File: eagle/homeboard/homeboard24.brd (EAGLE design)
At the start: 94 x 71.8 mm, 128 parts, among them IC1 XCF02S, IC2 25LC080SN, IC3 ATMEGA32U2-TQFP, Q5 BC848SMD, Q6 BC848SMD, Q7 BC848SMD, Q8 BC848SMD, T1 BSS138, T2 BC848, T3 BSS138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

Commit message: added text
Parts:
- removed C28, C30, C31: 100nF, rcl:C0603
- moved C13 36.1 mm to (64.5, 41.5), flipped to the bottom, turned to 180 degrees
- moved U$8 1.12 mm to (89.5, 51.0)
- moved R36 1.00 mm to (55.2, 54.5)
- moved R39 1.00 mm to (57.5, 54.5)
- moved R46 1.00 mm to (53.0, 54.5)
- moved U$7 0.50 mm to (4.50, 55.0)
- moved U$9 0.50 mm to (89.5, 10.0)
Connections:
- net GND: no longer C28.2, C30.2, C31.2
- net VCC: no longer C28.1, C30.1, C31.1
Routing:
- net GND: track 999.5 -> 1001.9 mm
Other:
- board text added: "#crtc"
- board text added: "(c) 2012 Ranulf Doswell"
- board text added: "-FPGA-XTAL-"
- board text added: "123"
- board text added: "127"
- board text added: "128"
- board text added: "129"
- board text added: "130"
- board text added: "132"
- board text added: "135"
- board text added: "137"
- board text added: "5V"
- board text added: "CPCFPGA.COM rev 1"
- board text added: "GND"
- board text added: "P47"
- board text added: "P50"
- board text added: "P51"
- board text added: "P74"
- board text added: "P76"
- board text added: "P77"
- board text added: "VCC"
- board text added: "VCCAUX"
- board text added: "VCCINT"

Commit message: mah
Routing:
- net VCC: track 533.5 -> 539.5 mm
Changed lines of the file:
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@@
 <wire x1="36.25" y1="44.75" x2="23.5" y2="44.75" width="0.7" layer="1"/>
 <wire x1="23.5" y1="44.75" x2="23.5" y2="47.5" width="0.7" layer="1"/>
-<wire x1="23.5" y1="47.5" x2="16.5" y2="47.5" width="0.7" layer="1"/>
+<wire x1="23.5" y1="47.5" x2="23.5" y2="53.55" width="0.7" layer="1"/>
 <wire x1="16.5" y1="47.5" x2="13" y2="47.5" width="0.7" layer="1"/>
 <wire x1="13" y1="47.5" x2="9.5" y2="47.5" width="0.8" layer="1"/>
@@
 <wire x1="83.5" y1="20.75" x2="85.5" y2="20.75" width="0.8" layer="1"/>
 <contactref element="SV4" pad="20"/>
-<wire x1="21.75" y1="53.55" x2="24" y2="53.55" width="0.7" layer="1"/>
+<wire x1="21.75" y1="53.55" x2="23.5" y2="53.55" width="0.7" layer="1"/>
+<wire x1="23.5" y1="53.55" x2="24" y2="53.55" width="0.7" layer="1"/>
 <wire x1="24" y1="53.55" x2="26.25" y2="53.55" width="0.7" layer="1"/>
 <wire x1="26.25" y1="53.55" x2="28.5" y2="53.55" width="0.7" layer="1"/>
@@
 <wire x1="64.5" y1="53.5" x2="64.7" y2="53.5" width="0.254" layer="1"/>
 <wire x1="64.7" y1="53.5" x2="64.75" y2="53.55" width="0.254" layer="1"/>
-<wire x1="37.5" y1="15.75" x2="37.52" y2="15.79" width="0" layer="19" extent="1-1"/>
-<wire x1="23.516" y1="17.9906" x2="23.5" y2="18" width="0" layer="19" extent="16-16"/>
+<wire x1="16.5" y1="47.5" x2="23.5" y2="47.5" width="0.6" layer="1"/>
+<wire x1="23.5" y1="18" x2="23.516" y2="17.9906" width="0" layer="19" extent="16-16"/>
 </signal>
 <signal name="TCK">

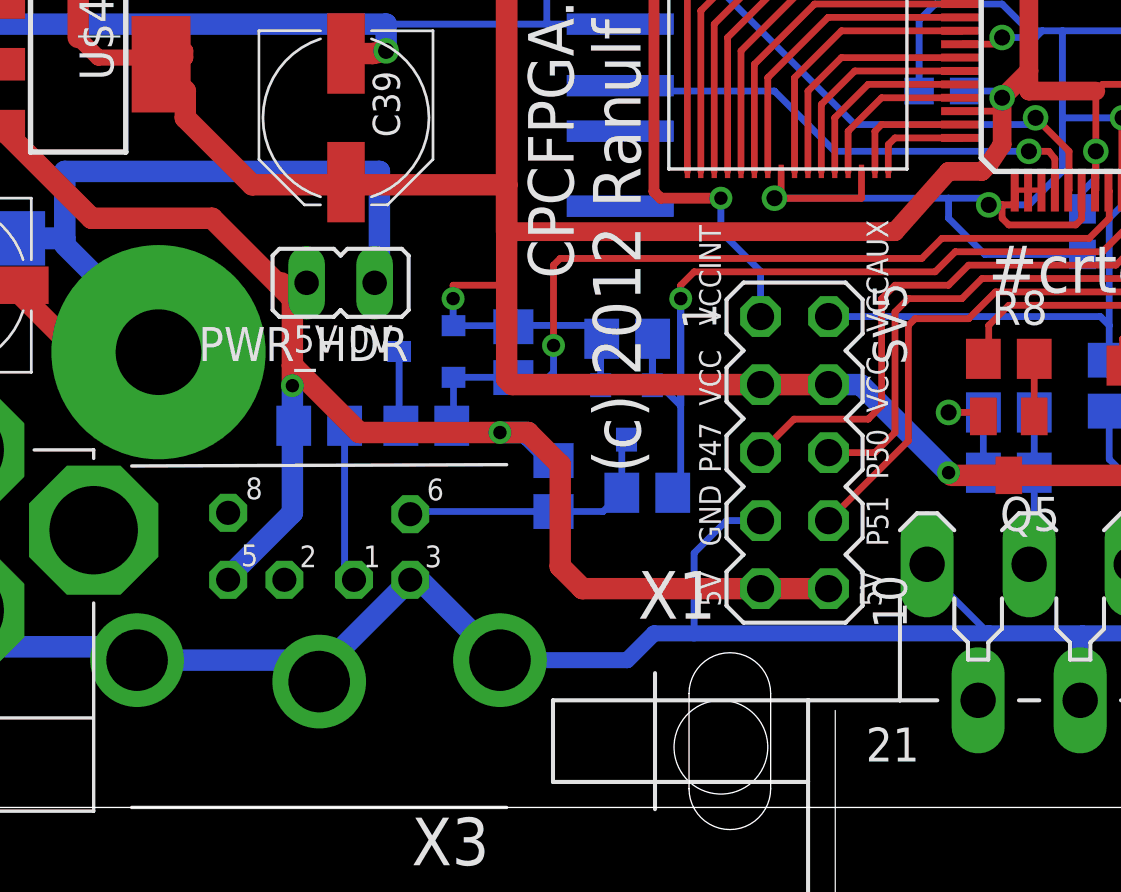
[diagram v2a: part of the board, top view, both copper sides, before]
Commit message: moved ps2 stuff to top layer
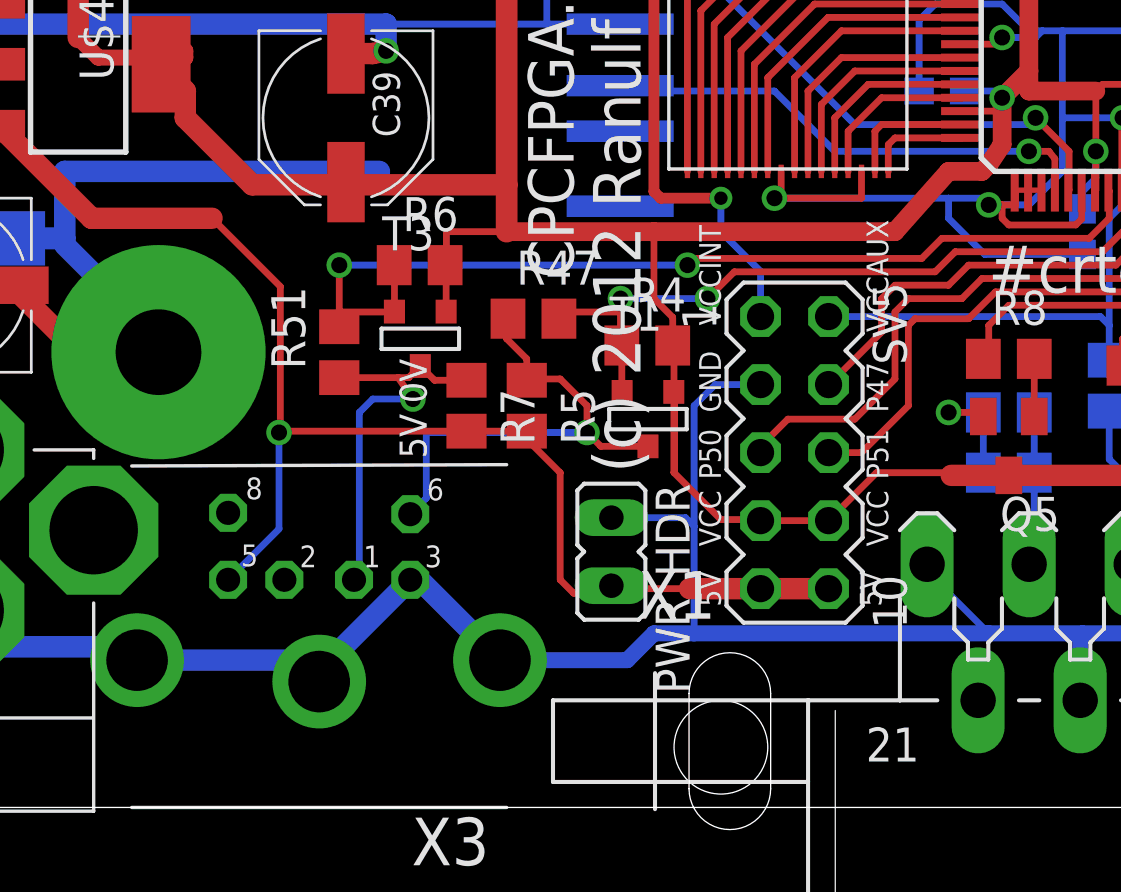
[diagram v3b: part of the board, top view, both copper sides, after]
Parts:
- moved PWR_HDR 14.2 mm to (29.4, 9.55), turned to 180 degrees
- moved R47 7.77 mm to (26.5, 18.2), flipped to the top, turned to 0 degrees
- moved R7 5.55 mm to (24.0, 15.0), flipped to the top, turned to 270 degrees
- moved R6 4.78 mm to (22.2, 20.2), flipped to the top, turned to 0 degrees
- moved R51 4.26 mm to (19.2, 17.0), flipped to the top, turned to 90 degrees
- moved R5 3.16 mm to (26.2, 15.0), flipped to the top, turned to 270 degrees
- moved R4 0.79 mm to (30.8, 17.2), flipped to the top
- moved T1 0.79 mm to (30.8, 14.5), flipped to the top
- moved T3 0.56 mm to (22.2, 17.5), flipped to the top, turned to 0 degrees
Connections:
- net EXP_A: now also SV5.4; no longer SV5.5
- net EXP_B: now also SV5.5; no longer SV5.6
- net EXP_C: now also SV5.6; no longer SV5.8
- net GND: now also SV5.3; no longer SV5.7
- net VCC: now also SV5.7, SV5.8; no longer SV5.3, SV5.4
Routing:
- net PS2CLK: track 35.6 -> 27.4 mm, vias 1 -> 2
- net CLK_5V: track 10.3 -> 18.1 mm, vias 0 -> 1
- net VCC: track 539.5 -> 532.9 mm, vias 26 -> 24
- net EXP_A: track 21.8 -> 16.6 mm
- net PS2DAT: track 32.5 -> 37.0 mm, vias 1 -> 2
- net GND: track 1001.9 -> 1006.1 mm
- net DATA_5V: track 11.0 -> 14.7 mm, vias 0 -> 1
- net VCC5: track 94.2 -> 90.7 mm, vias 2 -> 1
- net EXP_C: track 22.5 -> 20.7 mm
- net EXP_B: track 20.8 -> 22.3 mm

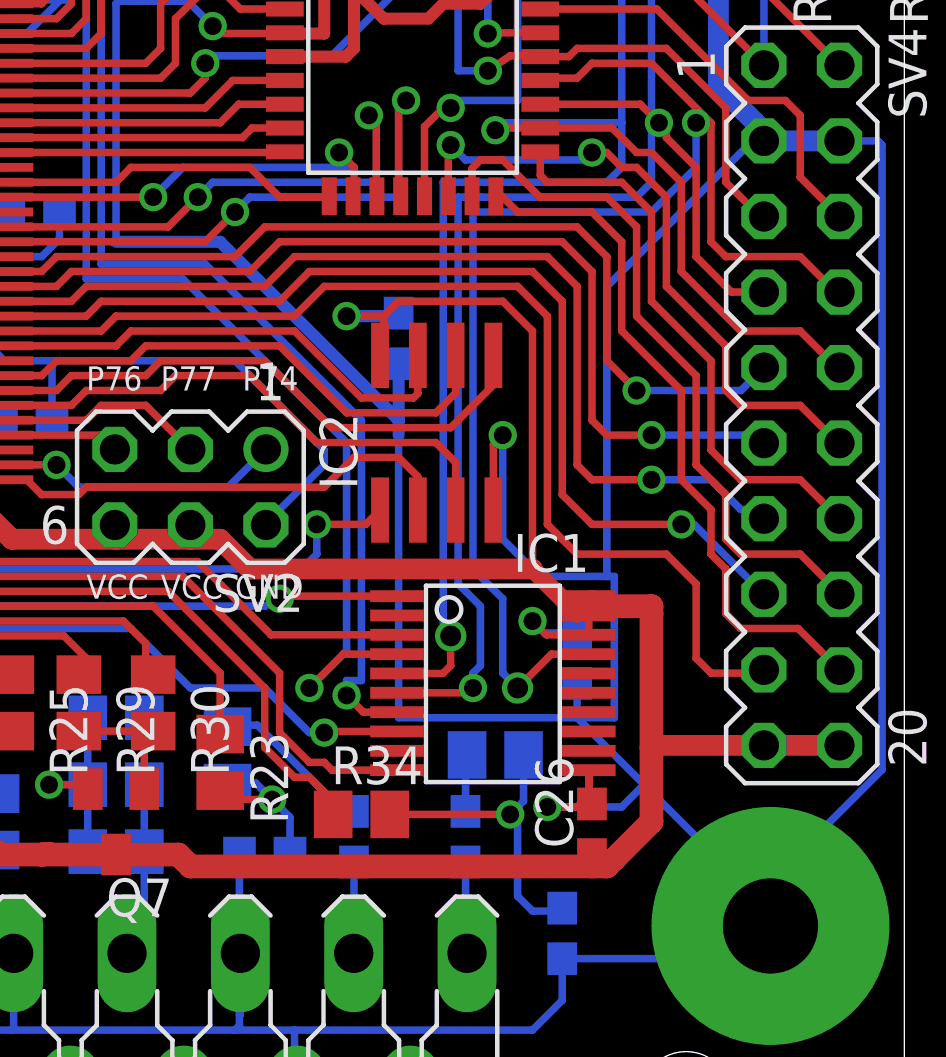
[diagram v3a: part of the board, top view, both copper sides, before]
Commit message: removed spare cap
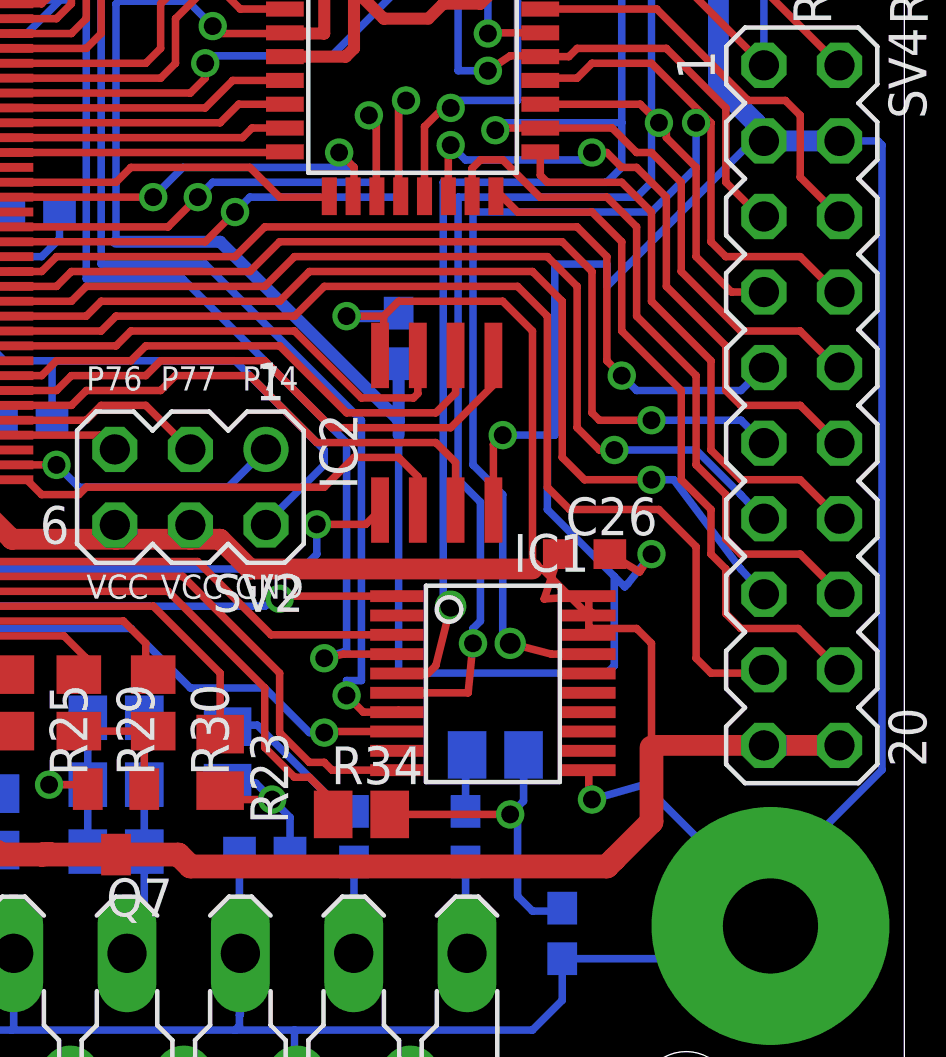
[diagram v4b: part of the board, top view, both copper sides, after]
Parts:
- removed C32: 100nF, rcl:C0603
- moved C26 9.25 mm to (83.2, 22.5), turned to 0 degrees
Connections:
- net GND: no longer C32.2
- net VCC: no longer C32.1
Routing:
- net GND: track 1006.1 -> 996.6 mm, vias 30 -> 31
- net VCC: track 532.9 -> 528.3 mm, vias 24 -> 23
- net TDO_FPGA: track 41.6 -> 39.7 mm
- net TDO_PROM: track 45.4 -> 43.6 mm
- net HDR_MISO: track 33.1 -> 32.4 mm

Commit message: moving around
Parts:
- moved R49 2.83 mm to (82.2, 13.8), turned to 90 degrees
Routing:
- net N$40: track 59.4 -> 66.0 mm
- net PROM_INITB: track 31.1 -> 33.5 mm
- net N$64: track 1.95 -> 4.13 mm
- net TCK: track 78.6 -> 79.6 mm
- net VCC: track 528.3 -> 527.3 mm
- net N$65: track 11.0 -> 10.0 mm
- net GND: track 996.6 -> 996.0 mm

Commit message: moving around
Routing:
- net PROM_INITB: track 33.5 -> 39.6 mm
- net N$38: track 20.6 -> 20.0 mm
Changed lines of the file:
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@@
 <via x="54" y="24.5" extent="1-16" drill="0.6" shape="square"/>
 <wire x1="54" y1="24.5" x2="54" y2="20" width="0.254" layer="16"/>
-<via x="75.25" y="16.5" extent="1-16" drill="0.6" shape="square"/>
 <wire x1="54" y1="20" x2="71.75" y2="20" width="0.254" layer="16"/>
-<wire x1="76.943396875" y1="16.537409375" x2="76.037409375" y2="16.537409375" width="0.254" layer="1"/>
-<wire x1="76.037409375" y1="16.537409375" x2="75.25" y2="16.5" width="0.254" layer="1"/>
-<wire x1="75.25" y1="16.5" x2="76.5" y2="16.5" width="0.254" layer="16"/>
 <wire x1="76.5" y1="16.5" x2="75" y2="18" width="0.254" layer="16"/>
 <wire x1="75" y1="18" x2="73.75" y2="18" width="0.254" layer="16"/>
@@
 <wire x1="54.97" y1="24.03" x2="54.5" y2="24.5" width="0.254" layer="1"/>
 <wire x1="54.5" y1="24.5" x2="54" y2="24.5" width="0.254" layer="1"/>
+<wire x1="76.5" y1="16.5" x2="80.5" y2="16.5" width="0.254" layer="16"/>
+<wire x1="80.5" y1="16.5" x2="81" y2="17" width="0.254" layer="16"/>
+<via x="81" y="17" extent="1-16" drill="0.6" shape="square"/>
+<wire x1="81" y1="17" x2="80.5" y2="16.5" width="0.254" layer="1"/>
+<wire x1="80.5" y1="16.5" x2="76.98080625" y2="16.5" width="0.254" layer="1"/>
+<wire x1="76.98080625" y1="16.5" x2="76.943396875" y2="16.537409375" width="0.254" layer="1"/>
 </signal>
 <signal name="N$39">
@@
 <contactref element="U1" pad="P110"/>
 <wire x1="61.47" y1="44.45" x2="61.47" y2="46.97" width="0.254" layer="1"/>
-<wire x1="61.47" y1="46.97" x2="63" y2="48.5" width="0.254" layer="1"/>
-<wire x1="63" y1="48.5" x2="62.75" y2="48.05" width="0" layer="19" extent="1-1"/>
+<wire x1="61.47" y1="46.97" x2="62.75" y2="48.25" width="0.254" layer="1"/>
+<wire x1="62.75" y1="48.25" x2="63" y2="48.5" width="0.254" layer="1"/>
+<wire x1="62.75" y1="48.05" x2="62.75" y2="48.25" width="0.254" layer="1"/>
 </signal>
 <signal name="N$42">
@@
 <wire x1="61.47" y1="23.05" x2="61.47" y2="21.78" width="0.254" layer="1"/>
 <wire x1="61.47" y1="21.78" x2="61.5" y2="21.75" width="0.254" layer="1"/>
-<wire x1="61.5" y1="21.75" x2="69.75" y2="21.75" width="0.254" layer="1"/>
-<wire x1="69.75" y1="21.75" x2="73" y2="18.5" width="0.254" layer="1"/>
-<wire x1="76.943396875" y1="15.237409375" x2="74.762590625" y2="15.237409375" width="0.254" layer="1"/>
-<wire x1="74.762590625" y1="15.237409375" x2="74.5" y2="15.5" width="0.254" layer="1"/>
-<wire x1="74.5" y1="15.5" x2="74" y2="15.5" width="0.254" layer="1"/>
-<wire x1="74" y1="15.5" x2="73" y2="16.5" width="0.254" layer="1"/>
-<wire x1="73" y1="16.5" x2="73" y2="18.5" width="0.254" layer="1"/>
+<wire x1="61.5" y1="21.75" x2="70" y2="21.75" width="0.254" layer="1"/>
+<wire x1="70" y1="21.75" x2="75.5" y2="16.25" width="0.254" layer="1"/>
+<wire x1="75.5" y1="16.25" x2="75.5" y2="15.25" width="0.254" layer="1"/>
+<wire x1="75.5" y1="15.25" x2="76.75" y2="15.25" width="0.254" layer="1"/>
+<wire x1="76.943396875" y1="15.237409375" x2="76.762590625" y2="15.237409375" width="0.254" layer="1"/>
+<wire x1="76.762590625" y1="15.237409375" x2="76.75" y2="15.25" width="0.254" layer="1"/>
 </signal>
 <signal name="N$40">
@@
 <wire x1="59" y1="25" x2="59.5" y2="24.5" width="0.254" layer="16"/>
 <wire x1="59.5" y1="24.5" x2="59.5" y2="20.75" width="0.254" layer="16"/>
-<wire x1="59.5" y1="20.75" x2="72.5" y2="20.75" width="0.254" layer="16"/>
-<wire x1="72.5" y1="20.75" x2="73" y2="21" width="0.254" layer="16"/>
+<wire x1="59.5" y1="20.75" x2="74" y2="20.75" width="0.254" layer="16"/>
+<wire x1="74" y1="20.75" x2="74.25" y2="21" width="0.254" layer="16"/>
 <wire x1="58.5" y1="22.52" x2="58.47" y2="23.05" width="0.254" layer="1"/>
 <wire x1="58.5" y1="22.52" x2="58.5" y2="25.25" width="0.254" layer="1"/>
 <wire x1="58.5" y1="25.25" x2="59" y2="25.25" width="0.254" layer="1"/>
-<via x="73" y="21" extent="1-16" drill="0.6" shape="square"/>
-<wire x1="76.943396875" y1="21.087409375" x2="73.337409375" y2="21.087409375" width="0.254" layer="1"/>
-<wire x1="73.337409375" y1="21.087409375" x2="73" y2="21" width="0.254" layer="1"/>
+<via x="74.25" y="21" extent="1-16" drill="0.6" shape="square"/>
+<wire x1="76.943396875" y1="21.087409375" x2="74.337409375" y2="21.087409375" width="0.254" layer="1"/>
+<wire x1="74.337409375" y1="21.087409375" x2="74.25" y2="21" width="0.254" layer="1"/>
 </signal>
 <signal name="VCCINT">

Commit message: moving around
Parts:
- removed SV4: (no value), con-lstb:MA10-2
- added SV1: (no value), con-lstb:MA10-2
- moved R23 29.1 mm to (100.0, 13.0)
- moved R48 25.9 mm to (96.8, 11.2), flipped to the top, turned to 180 degrees
- moved C1 25.8 mm to (98.0, 8.50), flipped to the top, turned to 90 degrees
- moved C3 20.5 mm to (95.5, 8.50), flipped to the top
- moved C4 10.3 mm to (80.5, 2.75), flipped to the top, turned to 180 degrees
- moved R49 10.0 mm to (83.2, 3.75), flipped to the top, turned to 270 degrees
- moved R34 9.60 mm to (83.2, 7.75), turned to 270 degrees
- moved C5 5.15 mm to (80.5, 5.00), flipped to the top, turned to 0 degrees
- moved R56 2.02 mm to (92.0, 44.8)
- moved R55 2.00 mm to (89.0, 44.8)
- moved R30 0.75 mm to (68.0, 17.5)
- moved R24 0.50 mm to (60.2, 17.8)
- moved R25 0.50 mm to (63.5, 17.5)
- moved R29 0.50 mm to (65.8, 17.5)
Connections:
- net AT_RESET: now also SV1.2; no longer SV4.1
- net EMER_BOOT: now also SV1.1; no longer SV4.2
- net GND: now also SV1.5, SV1.6; no longer SV4.3, SV4.4
- net HDR_MISO: now also SV1.15; no longer SV4.13
- net HDR_MOSI: now also SV1.19; no longer SV4.17
- net HDR_SCLK: now also SV1.17; no longer SV4.15
- net HDR_SEL: now also SV1.13; no longer SV4.11
- net HDR_SPARE: now also SV1.11; no longer SV4.9
- net SPI_MISO: now also SV1.16; no longer SV4.14
- net SPI_MOSI: now also SV1.20; no longer SV4.18
- net SPI_SCLK: now also SV1.18; no longer SV4.16
- net SPI_SEL: now also SV1.14; no longer SV4.12
- net TCK: now also SV1.9; no longer SV4.7
- net TDI_FPGA: now also SV1.7; no longer SV4.5
- net TDO_EXP: now also SV1.8; no longer SV4.6
- net TDO_PROM: now also SV1.10; no longer SV4.8
- net TMS: now also SV1.12; no longer SV4.10
- net VCC: now also SV1.3, SV1.4; no longer SV4.19, SV4.20
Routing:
- net VCC: track 527.3 -> 559.3 mm
- net GND: track 996.0 -> 983.6 mm
- net N$65: track 10.0 -> 0.00 mm, vias 1 -> 0
- net FPGA_AUDIO_RIGHT: track 21.3 -> 15.0 mm
- net N$51: track 5.58 -> 0.00 mm, vias 1 -> 0
- net N$52: track 5.47 -> 0.00 mm
- net N$64: track 4.13 -> 0.00 mm
- net EMER_BOOT: track 24.9 -> 21.3 mm
- net SCART_LEFT: track 3.23 -> 0.00 mm
- net SCART_RIGHT: track 3.09 -> 0.00 mm
- net FPGA_AUDIO_LEFT: track 16.1 -> 14.1 mm
- net AT_RESET: track 15.3 -> 13.5 mm, vias 1 -> 0
- net B1: track 13.9 -> 13.0 mm
- net HDR_MOSI: track 37.0 -> 37.6 mm
